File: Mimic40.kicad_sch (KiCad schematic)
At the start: 11 parts, among them J3 Conn_01x03, J4 Conn_01x04

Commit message: plate + usb soldermask fix
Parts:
- added N1: Plate, symbol Mechanical:Housing
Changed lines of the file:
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@@
+	)
+	(symbol
+		(lib_id "Mechanical:Housing")
+		(at 21.59 254 0)
+		(unit 1)
+		(exclude_from_sim yes)
+		(in_bom no)
+		(on_board no)
+		(dnp no)
+		(fields_autoplaced yes)
+		(property "Reference" "N1"
+			(at 25.4 253.0474 0)
+			(effects
+				(font
+					(size 1.27 1.27)
+				)
+				(justify left)
+			)
+		)
+		(property "Value" "Plate"
+			(at 25.4 255.5874 0)
+			(effects
+				(font
+					(size 1.27 1.27)
+				)
+				(justify left)
+			)
+		)
+		(property "Footprint" ""
+			(at 22.86 252.73 0)
+			(effects
+				(font
+					(size 1.27 1.27)
+				)
+				(hide yes)
+			)
+		)
+		(property "Datasheet" "~"
+			(at 22.86 252.73 0)
+			(effects
+				(font
+					(size 1.27 1.27)
+				)
+				(hide yes)
+			)
+		)
+		(property "Description" "Housing"
+			(at 21.59 254 0)
+			(effects
+				(font
+					(size 1.27 1.27)
+				)
+				(hide yes)
+			)
+		)
+		(instances
+			(project ""
+				(path "/e63e39d7-6ac0-4ffd-8aa3-1841a4541b55"
+					(reference "N1")
+					(unit 1)
+				)
+			)
+		)
 	)
 	(symbol

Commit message: add part nums for bom
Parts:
- H1, H2, H3, H4, H5, H6, H7, H8, H9: now left out of the parts list
- J3, J4: Type (none) -> DNS

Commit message: usb changes for high power (leds)
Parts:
- renumbered H7 to H2, H2 to H3, H9 to H4, H4 to H5, H3 to H6, H5 to H7, H6 to H8, H8 to H9, J4 to J3, J3 to J5
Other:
- title: "not-so-fullsize" ortho -> Mimic40
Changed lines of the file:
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@@
 	(paper "A3")
 	(title_block
-		(title "\"not-so-fullsize\" ortho")
-		(date "2024-08-07")
-		(rev "2")
-		(comment 1 "Author: Kev")
+		(title "Mimic40")
+		(date "2024-09-22")
+		(rev "3")
+		(comment 1 "Author: kevontheweb")
 	)
 	(no_connect
@@
 		(on_board yes)
 		(dnp no)
-		(property "Reference" "H2"
+		(property "Reference" "H3"
 			(at 21.59 278.2316 0)
 			(effects
@@
 			(project "Mimic40"
 				(path "/e63e39d7-6ac0-4ffd-8aa3-1841a4541b55"
-					(reference "H2")
+					(reference "H3")
 					(unit 1)
 				)
@@
 		(on_board yes)
 		(dnp no)
-		(property "Reference" "H4"
+		(property "Reference" "H5"
 			(at 43.18 266.8016 0)
 			(effects
@@
 			(project "Mimic40"
 				(path "/e63e39d7-6ac0-4ffd-8aa3-1841a4541b55"
-					(reference "H4")
+					(reference "H5")
 					(unit 1)
 				)
@@
 		(on_board yes)
 		(dnp no)
-		(property "Reference" "H3"
+		(property "Reference" "H6"
 			(at 43.18 278.2316 0)
 			(effects
@@
 			(project "Mimic40"
 				(path "/e63e39d7-6ac0-4ffd-8aa3-1841a4541b55"
-					(reference "H3")
+					(reference "H6")
+					(unit 1)
+				)
+			)
+		)
+	)
+	(symbol
+		(lib_id "power:PWR_FLAG")
+		(at 200.66 245.11 0)
+		(unit 1)
+		(exclude_from_sim no)
+		(in_bom yes)
+		(on_board yes)
+		(dnp no)
+		(fields_autoplaced yes)
+		(property "Reference" "#FLG02"
+			(at 200.66 243.205 0)
+			(effects
+				(font
+					(size 1.27 1.27)
+				)
+				(hide yes)
+			)
+		)
+		(property "Value" "PWR_FLAG"
+			(at 200.66 240.03 0)
+			(effects
+				(font
+					(size 1.27 1.27)
+				)
+			)
+		)
+		(property "Footprint" ""
+			(at 200.66 245.11 0)
+			(effects
+				(font
+					(size 1.27 1.27)
+				)
+				(hide yes)
+			)
+		)
+		(property "Datasheet" "~"
+			(at 200.66 245.11 0)
+			(effects
+				(font
+					(size 1.27 1.27)
+				)
+				(hide yes)
+			)
+		)
+		(property "Description" "Special symbol for telling ERC where power comes from"
+			(at 200.66 245.11 0)
+			(effects
+				(font
+					(size 1.27 1.27)
+				)
+				(hide yes)
+			)
+		)
+		(pin "1"
+		)
+		(instances
+			(project "Mimic40"
+				(path "/e63e39d7-6ac0-4ffd-8aa3-1841a4541b55"
+					(reference "#FLG02")
 					(unit 1)
 				)
@@
 		(on_board yes)
 		(dnp no)
-		(property "Reference" "H9"
+		(property "Reference" "H4"
 			(at 104.14 266.8016 0)
 			(effects
@@
 			(project "Mimic40"
 				(path "/e63e39d7-6ac0-4ffd-8aa3-1841a4541b55"
-					(reference "H9")
+					(reference "H4")
 					(unit 1)
 				)
@@
 		(on_board yes)
 		(dnp no)
-		(property "Reference" "H6"
+		(property "Reference" "H8"
 			(at 63.5 278.2316 0)
 			(effects
@@
 			(project "Mimic40"
 				(path "/e63e39d7-6ac0-4ffd-8aa3-1841a4541b55"
-					(reference "H6")
-					(unit 1)
-				)
-			)
-		)
-	)
-	(symbol
-		(lib_id "PCM_4ms_Power-symbol:PWR_FLAG")
-		(at 200.66 245.11 0)
-		(unit 1)
-		(exclude_from_sim no)
-		(in_bom yes)
-		(on_board yes)
-		(dnp no)
-		(fields_autoplaced yes)
-		(property "Reference" "#FLG02"
-			(at 200.66 243.205 0)
-			(effects
-				(font
-					(size 1.27 1.27)
-				)
-				(hide yes)
-			)
-		)
-		(property "Value" "PWR_FLAG"
-			(at 200.66 240.03 0)
-			(effects
-				(font
-					(size 1.27 1.27)
-				)
-			)
-		)
-		(property "Footprint" ""
-			(at 200.66 245.11 0)
-			(effects
-				(font
-					(size 1.27 1.27)
-				)
-				(hide yes)
-			)
-		)
-		(property "Datasheet" ""
-			(at 200.66 245.11 0)
-			(effects
-				(font
-					(size 1.27 1.27)
-				)
-				(hide yes)
-			)
-		)
-		(property "Description" ""
-			(at 200.66 245.11 0)
-			(effects
-				(font
-					(size 1.27 1.27)
-				)
-				(hide yes)
-			)
-		)
-		(pin "1"
-		)
-		(instances
-			(project "Mimic40"
-				(path "/e63e39d7-6ac0-4ffd-8aa3-1841a4541b55"
-					(reference "#FLG02")
+					(reference "H8")
 					(unit 1)
 				)
@@
 		(on_board yes)
 		(dnp no)
-		(property "Reference" "H7"
+		(property "Reference" "H2"
 			(at 83.82 266.8016 0)
 			(effects
@@
 			(project "Mimic40"
 				(path "/e63e39d7-6ac0-4ffd-8aa3-1841a4541b55"
-					(reference "H7")
+					(reference "H2")
 					(unit 1)
 				)
@@
 		(on_board yes)
 		(dnp no)
-		(property "Reference" "H8"
+		(property "Reference" "H9"
 			(at 83.82 278.2316 0)
 			(effects
@@
 			(project "Mimic40"
 				(path "/e63e39d7-6ac0-4ffd-8aa3-1841a4541b55"
-					(reference "H8")
+					(reference "H9")
 					(unit 1)
 				)
@@
 		(on_board yes)
 		(dnp no)
-		(property "Reference" "H5"
+		(property "Reference" "H7"
 			(at 63.5 266.8016 0)
 			(effects
@@
 			(project "Mimic40"
 				(path "/e63e39d7-6ac0-4ffd-8aa3-1841a4541b55"
-					(reference "H5")
+					(reference "H7")
 					(unit 1)
 				)
@@
 		(dnp yes)
 		(fields_autoplaced yes)
-		(property "Reference" "J3"
+		(property "Reference" "J5"
 			(at 234.95 207.01 0)
 			(effects
@@
 			(project "Mimic40"
 				(path "/e63e39d7-6ac0-4ffd-8aa3-1841a4541b55"
-					(reference "J3")
+					(reference "J5")
 					(unit 1)
 				)
@@
 		(dnp yes)
 		(fields_autoplaced yes)
-		(property "Reference" "J4"
+		(property "Reference" "J3"
 			(at 149.86 204.47 0)
 			(effects
@@
 			(project "Mimic40"
 				(path "/e63e39d7-6ac0-4ffd-8aa3-1841a4541b55"
-					(reference "J4")
+					(reference "J3")
 					(unit 1)
 				)

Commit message: bulk cap and level shifter (still need to lay out)
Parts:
- H1, H2, H3, H4, H5, H6, H7, H8, H9, N1: MPN (none) -> DNP; now not fitted
- J3, J5: MPN (none) -> DNP
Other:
- added sheet Logic level shifter (Level Shifter.kicad_sch)
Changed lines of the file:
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@@
 	)
 	(no_connect
-		(at 172.72 151.13)
+		(at 134.62 151.13)
 	)
 	(no_connect
@@
 		)
 	)
-	(label "D_IN"
-		(at 172.72 148.59 0)
-		(fields_autoplaced yes)
-		(effects
-			(font
-				(size 1.27 1.27)
-			)
-			(justify left bottom)
-		)
-	)
 	(label "SWCLK"
 		(at 228.6 171.45 270)
@@
 		)
 	)
+	(label "D_LED_LV"
+		(at 152.4 144.78 180)
+		(fields_autoplaced yes)
+		(effects
+			(font
+				(size 1.27 1.27)
+			)
+			(justify right bottom)
+		)
+	)
 	(label "Col_1"
 		(at 203.2 166.37 180)
@@
 	)
 	(label "USB_D+"
-		(at 127 147.32 180)
+		(at 88.9 147.32 180)
 		(fields_autoplaced yes)
 		(effects
@@
 		)
 	)
+	(label "D_LED_HV"
+		(at 134.62 148.59 0)
+		(fields_autoplaced yes)
+		(effects
+			(font
+				(size 1.27 1.27)
+			)
+			(justify left bottom)
+		)
+	)
 	(label "Row_3"
 		(at 250.19 163.83 0)
@@
 	)
 	(label "USB_D-"
-		(at 127 149.86 180)
+		(at 88.9 149.86 180)
 		(fields_autoplaced yes)
 		(effects
@@
 		)
 	)
+	(label "D_LED_HV"
+		(at 172.72 144.78 0)
+		(fields_autoplaced yes)
+		(effects
+			(font
+				(size 1.27 1.27)
+			)
+			(justify left bottom)
+		)
+	)
 	(label "Row_2"
 		(at 250.19 161.29 0)
@@
 		)
 	)
-	(label "D_IN"
+	(label "D_LED_LV"
 		(at 203.2 146.05 180)
 		(fields_autoplaced yes)
@@
 		(in_bom no)
 		(on_board yes)
-		(dnp no)
+		(dnp yes)
 		(property "Reference" "H3"
 			(at 21.59 278.2316 0)
@@
 			)
 		)
-		(property "MPN" ""
+		(property "MPN" "DNP"
 			(at 19.05 279.4 0)
 			(effects
@@
 		(in_bom no)
 		(on_board yes)
-		(dnp no)
+		(dnp yes)
 		(property "Reference" "H1"
 			(at 21.59 266.8016 0)
@@
 			)
 		)
-		(property "MPN" ""
+		(property "MPN" "DNP"
 			(at 19.05 267.97 0)
 			(effects
@@
 		(in_bom no)
 		(on_board yes)
-		(dnp no)
+		(dnp yes)
 		(property "Reference" "H5"
 			(at 43.18 266.8016 0)
@@
 			)
 		)
-		(property "MPN" ""
+		(property "MPN" "DNP"
 			(at 40.64 267.97 0)
 			(effects
@@
 		(in_bom no)
 		(on_board yes)
-		(dnp no)
+		(dnp yes)
 		(property "Reference" "H6"
 			(at 43.18 278.2316 0)
@@
 			)
 		)
-		(property "MPN" ""
+		(property "MPN" "DNP"
 			(at 40.64 279.4 0)
 			(effects
@@
 		(in_bom no)
 		(on_board yes)
-		(dnp no)
+		(dnp yes)
 		(property "Reference" "H4"
 			(at 104.14 266.8016 0)
@@
 			)
 		)
-		(property "MPN" ""
+		(property "MPN" "DNP"
 			(at 101.6 267.97 0)
 			(effects
@@
 		(in_bom no)
 		(on_board yes)
-		(dnp no)
+		(dnp yes)
 		(property "Reference" "H8"
 			(at 63.5 278.2316 0)
@@
 			)
 		)
-		(property "MPN" ""
+		(property "MPN" "DNP"
 			(at 60.96 279.4 0)
 			(effects
@@
 		(in_bom no)
 		(on_board yes)
-		(dnp no)
+		(dnp yes)
 		(property "Reference" "H2"
 			(at 83.82 266.8016 0)
@@
 			)
 		)
-		(property "MPN" ""
+		(property "MPN" "DNP"
 			(at 81.28 267.97 0)
 			(effects
@@
 		(in_bom no)
 		(on_board yes)
-		(dnp no)
+		(dnp yes)
 		(property "Reference" "H9"
 			(at 83.82 278.2316 0)
@@
 			)
 		)
-		(property "MPN" ""
+		(property "MPN" "DNP"
 			(at 81.28 279.4 0)
 			(effects
@@
 		(in_bom no)
 		(on_board no)
-		(dnp no)
+		(dnp yes)
 		(fields_autoplaced yes)
 		(property "Reference" "N1"
@@
 			)
 		)
-		(property "MPN" ""
+		(property "MPN" "DNP"
 			(at 21.59 254 0)
 			(effects
@@
 		(in_bom no)
 		(on_board yes)
-		(dnp no)
+		(dnp yes)
 		(property "Reference" "H7"
 			(at 63.5 266.8016 0)
@@
 			)
 		)
-		(property "MPN" ""
+		(property "MPN" "DNP"
 			(at 60.96 267.97 0)
 			(effects
@@
 			)
 		)
-		(property "MPN" ""
+		(property "MPN" "DNP"
 			(at 234.95 215.9 0)
 			(effects
@@
 			)
 		)
-		(property "MPN" ""
+		(property "MPN" "DNP"
 			(at 149.86 215.9 0)
 			(effects
@@
 	)
 	(sheet
-		(at 127 139.7)
+		(at 88.9 139.7)
 		(size 20.32 17.78)
 		(fields_autoplaced yes)
@@
 		)
 		(property "Sheetname" "USB"
-			(at 127 138.3534 0)
+			(at 88.9 138.3534 0)
 			(effects
 				(font
@@
 		)
 		(property "Sheetfile" "USB.kicad_sch"
-			(at 127 158.0646 0)
+			(at 88.9 158.0646 0)
 			(effects
 				(font
@@
 		)
 		(pin "USB_D-" input
-			(at 127 149.86 180)
+			(at 88.9 149.86 180)
 			(effects
 				(font
@@
 		)
 		(pin "USB_D+" input
-			(at 127 147.32 180)
+			(at 88.9 147.32 180)
 			(effects
 				(font
@@
 	)
 	(sheet
-		(at 152.4 139.7)
+		(at 114.3 139.7)
 		(size 20.32 17.78)
 		(fields_autoplaced yes)
@@
 		)
 		(property "Sheetname" "LEDs"
-			(at 152.4 138.3534 0)
+			(at 114.3 138.3534 0)
 			(effects
 				(font
@@
 		)
 		(property "Sheetfile" "LEDs.kicad_sch"
-			(at 152.4 158.0646 0)
+			(at 114.3 158.0646 0)
 			(effects
 				(font
@@
 		)
 		(pin "D_IN" input
-			(at 172.72 148.59 0)
+			(at 134.62 148.59 0)
 			(effects
 				(font
@@
 		)
 		(pin "D_OUT" input
-			(at 172.72 151.13 0)
+			(at 134.62 151.13 0)
 			(effects
 				(font
@@
 				)
 			)
+		)
+	)
+	(sheet
+		(at 152.4 139.7)
+		(size 20.32 17.78)
+		(fields_autoplaced yes)
+		(stroke
+			(width 0.1524)
+			(type solid)
+		)
+		(fill
+			(color 0 0 0 0.0000)
+		)
+		(property "Sheetname" "Logic level shifter"
+			(at 152.4 138.3534 0)
+			(effects
+				(font
+					(size 2.54 2.54)
+					(bold yes)
+				)
+				(justify left bottom)
+			)
+		)
+		(property "Sheetfile" "Level Shifter.kicad_sch"
+			(at 152.4 158.0646 0)
+			(effects
+				(font
+					(size 1.27 1.27)
+				)
+				(justify left top)
+			)
+		)
+		(pin "3.3V" input
+			(at 152.4 144.78 180)
+			(effects
+				(font
+					(size 1.27 1.27)
+				)
+				(justify left)
+			)
+		)
+		(pin "5V" output
+			(at 172.72 144.78 0)
+			(effects
+				(font
+					(size 1.27 1.27)
+				)
+				(justify right)
+			)
+		)
+		(instances
+			(project "Mimic40"
+				(path "/e63e39d7-6ac0-4ffd-8aa3-1841a4541b55"
+					(page "6")
+				)
+			)

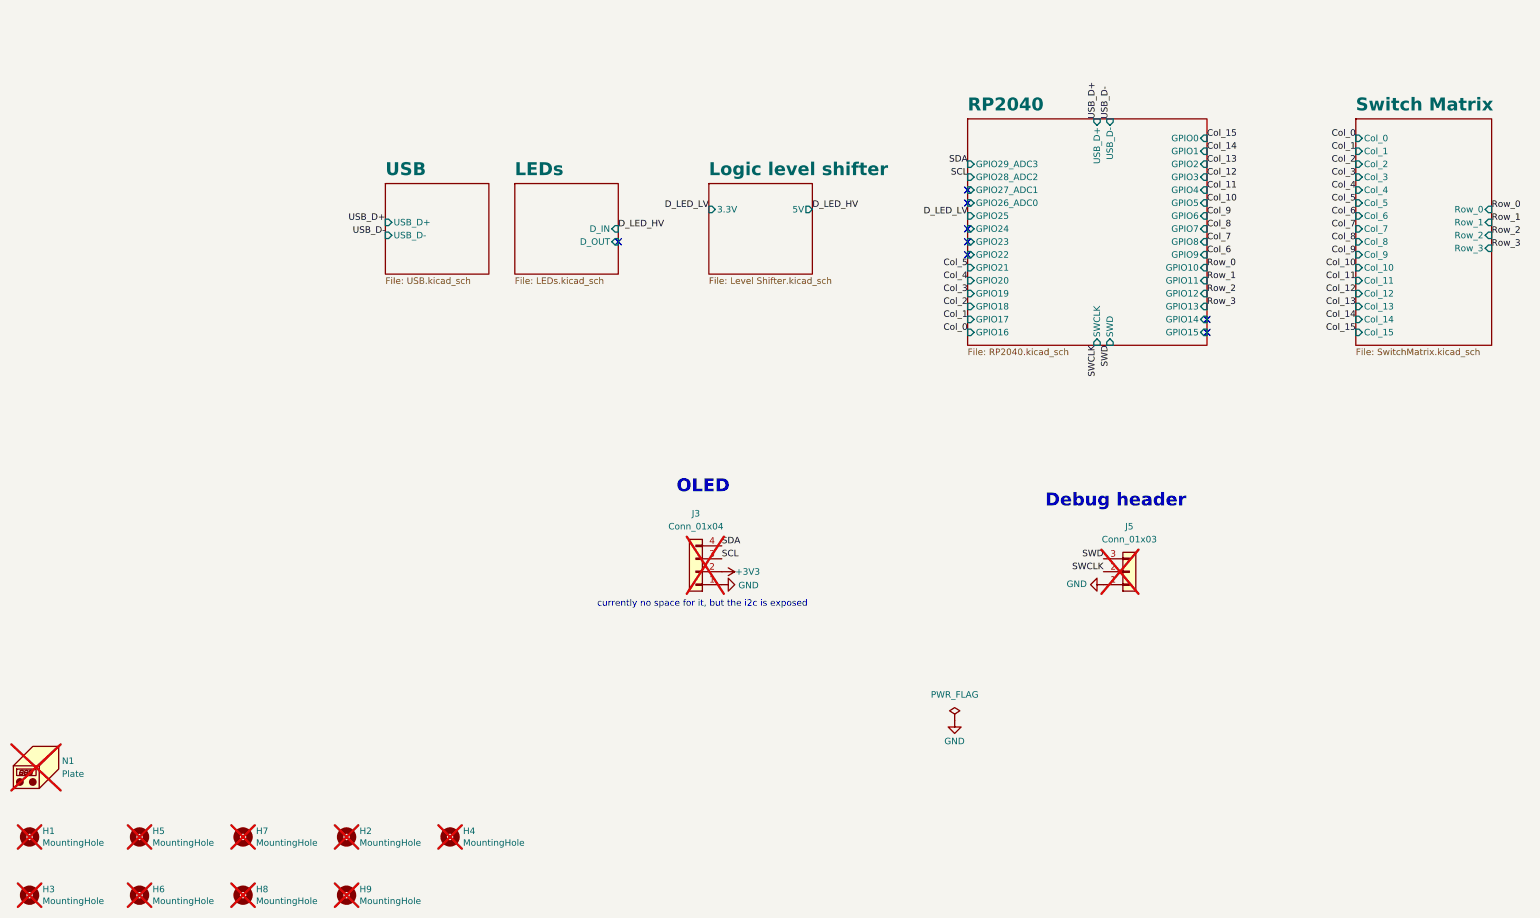
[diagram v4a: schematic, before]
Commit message: bulk caps for power (todo, split 470uF cap so that it can be shorter)
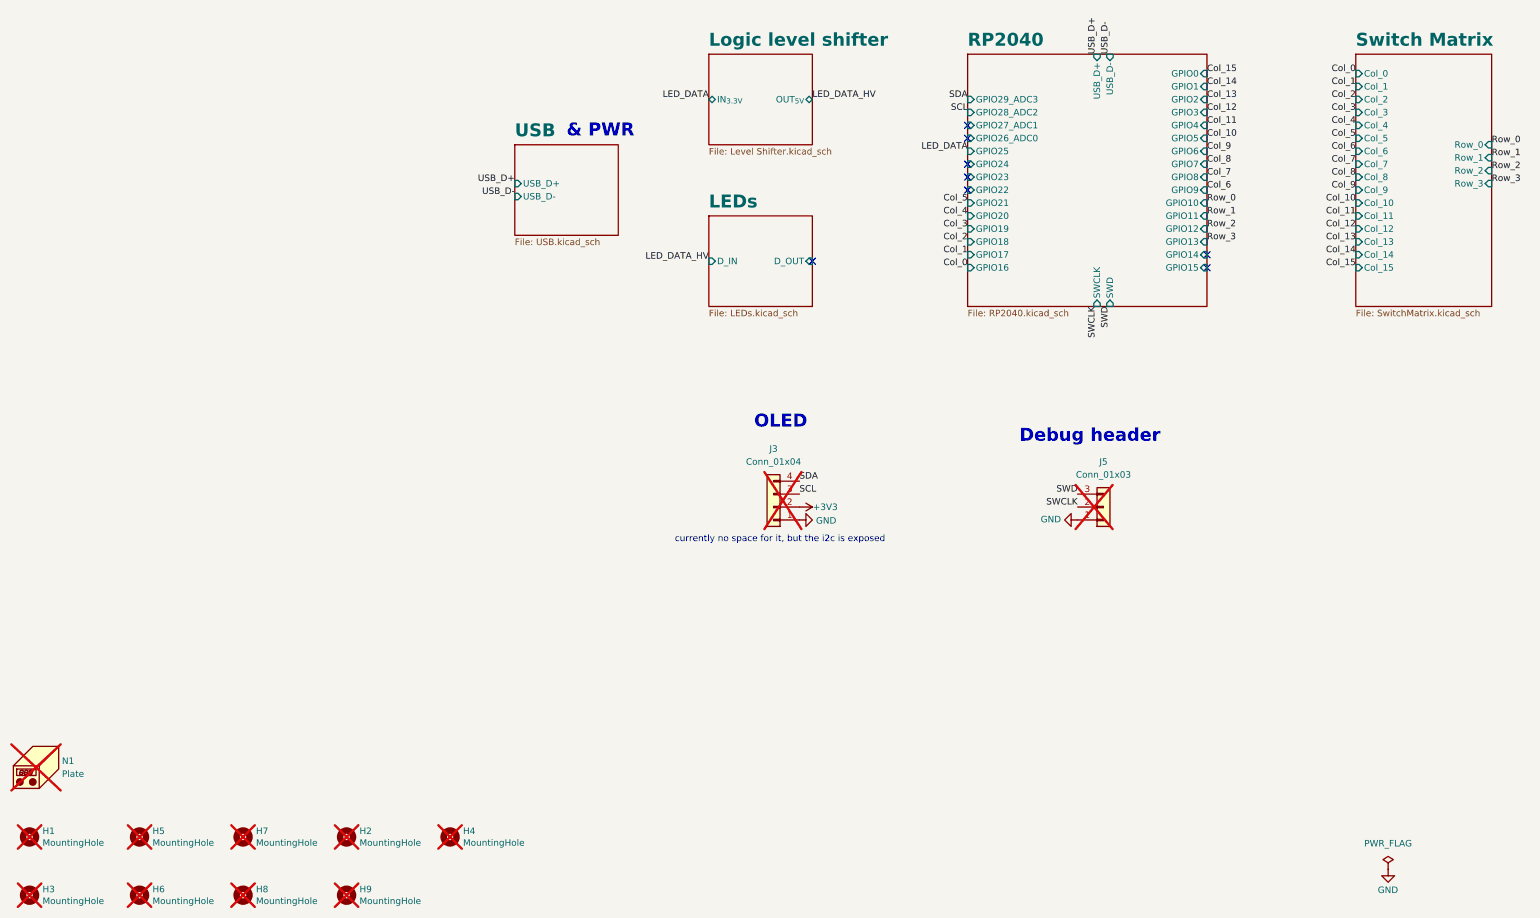
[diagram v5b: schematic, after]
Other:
- sheet Logic level shifter ports: added IN_{3.3V}, OUT_{5V}; removed 3.3V, 5V
- note added: "& PWR"
- moved on the sheet: J3, J5

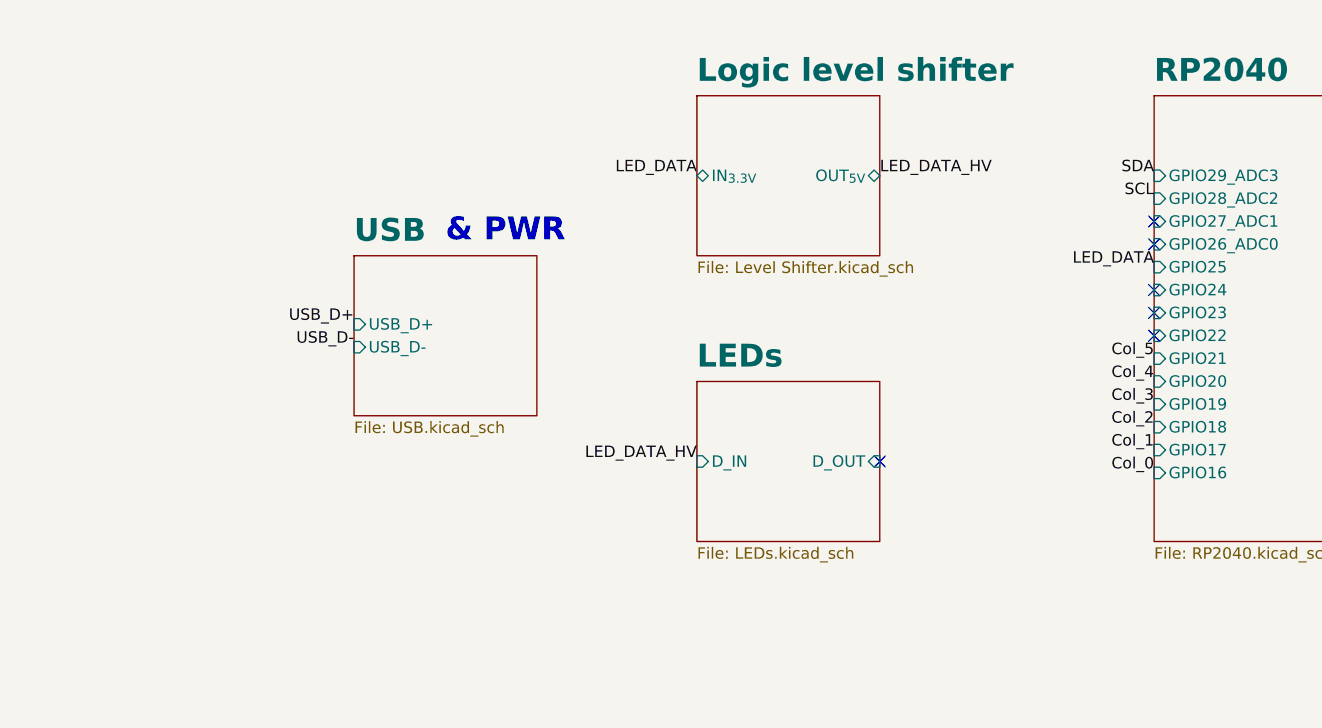
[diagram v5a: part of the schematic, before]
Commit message: add debug led, make bulk caps smaller, export plate and bottom for rudimentary case
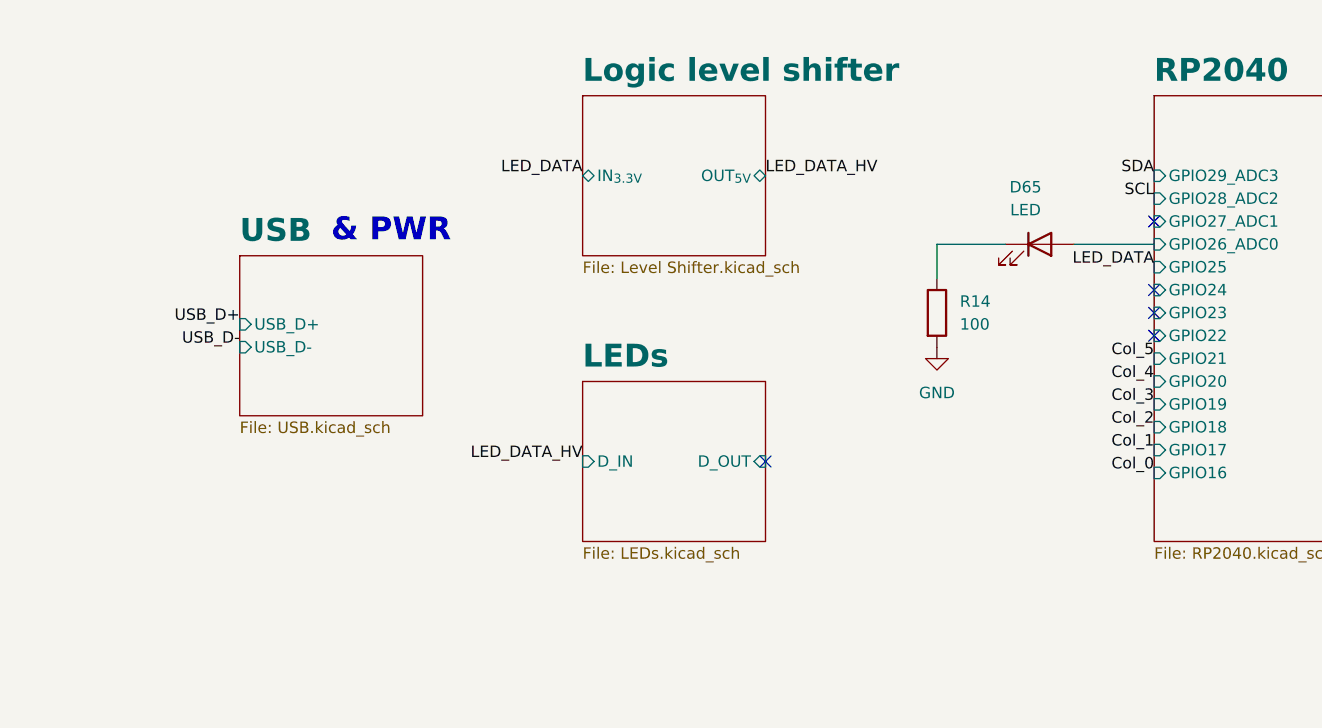
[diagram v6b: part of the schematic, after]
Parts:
- added D65: LED, LED_SMD:LED_0402_1005Metric, symbol Device:LED
- added R14: 100, Resistor_SMD:R_0402_1005Metric, symbol Device:R
- H1, H2, H3, H4, H5, H6, H7, H8, H9: footprint MountingHole:MountingHole_2.2mm_M2 -> kbd:MountingHole_5.3mm_M5
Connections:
- net GND: now also R14.2
- net RP2040/GPIO26_ADC0: now also D65.2 (A)
- new net: D65.1 (K), R14.1
- no-connect marks 8 -> 7
